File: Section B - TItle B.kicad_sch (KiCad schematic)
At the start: 0 parts

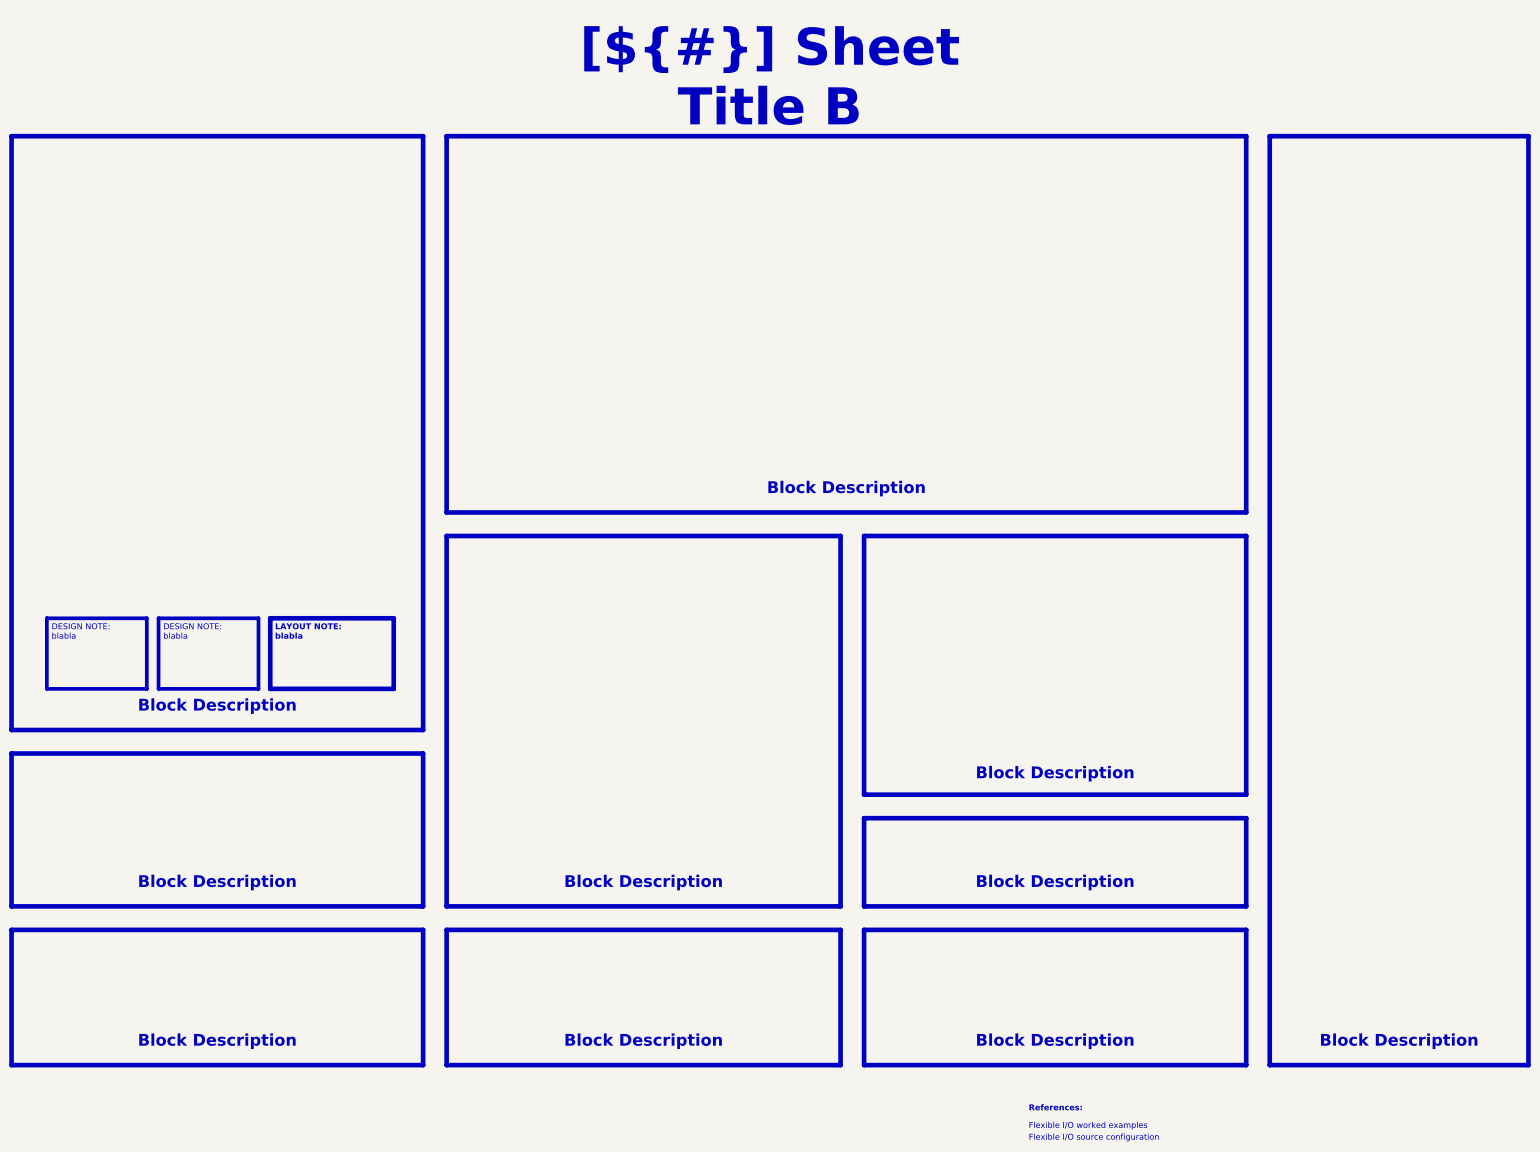
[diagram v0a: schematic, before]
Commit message: Save KiCad 10 design work
Snapshot of the schematic and PCB work done since the initial template
commit: AD7606C-18 ADC, 3x INA241A2 + PBV 1 mOhm shunts, MR60PW phase
connectors, LT8362 boost and LT3045-1 / LTC6655 analog supplies, project
libraries (lib/) and their sym/fp-lib-table.

.gitignore now excludes local history, SpinRender working files, the
stray .step export and Component Search Engine download leftovers.

Co-Authored-By: Claude Opus 5.5 <noreply@anthropic.com>
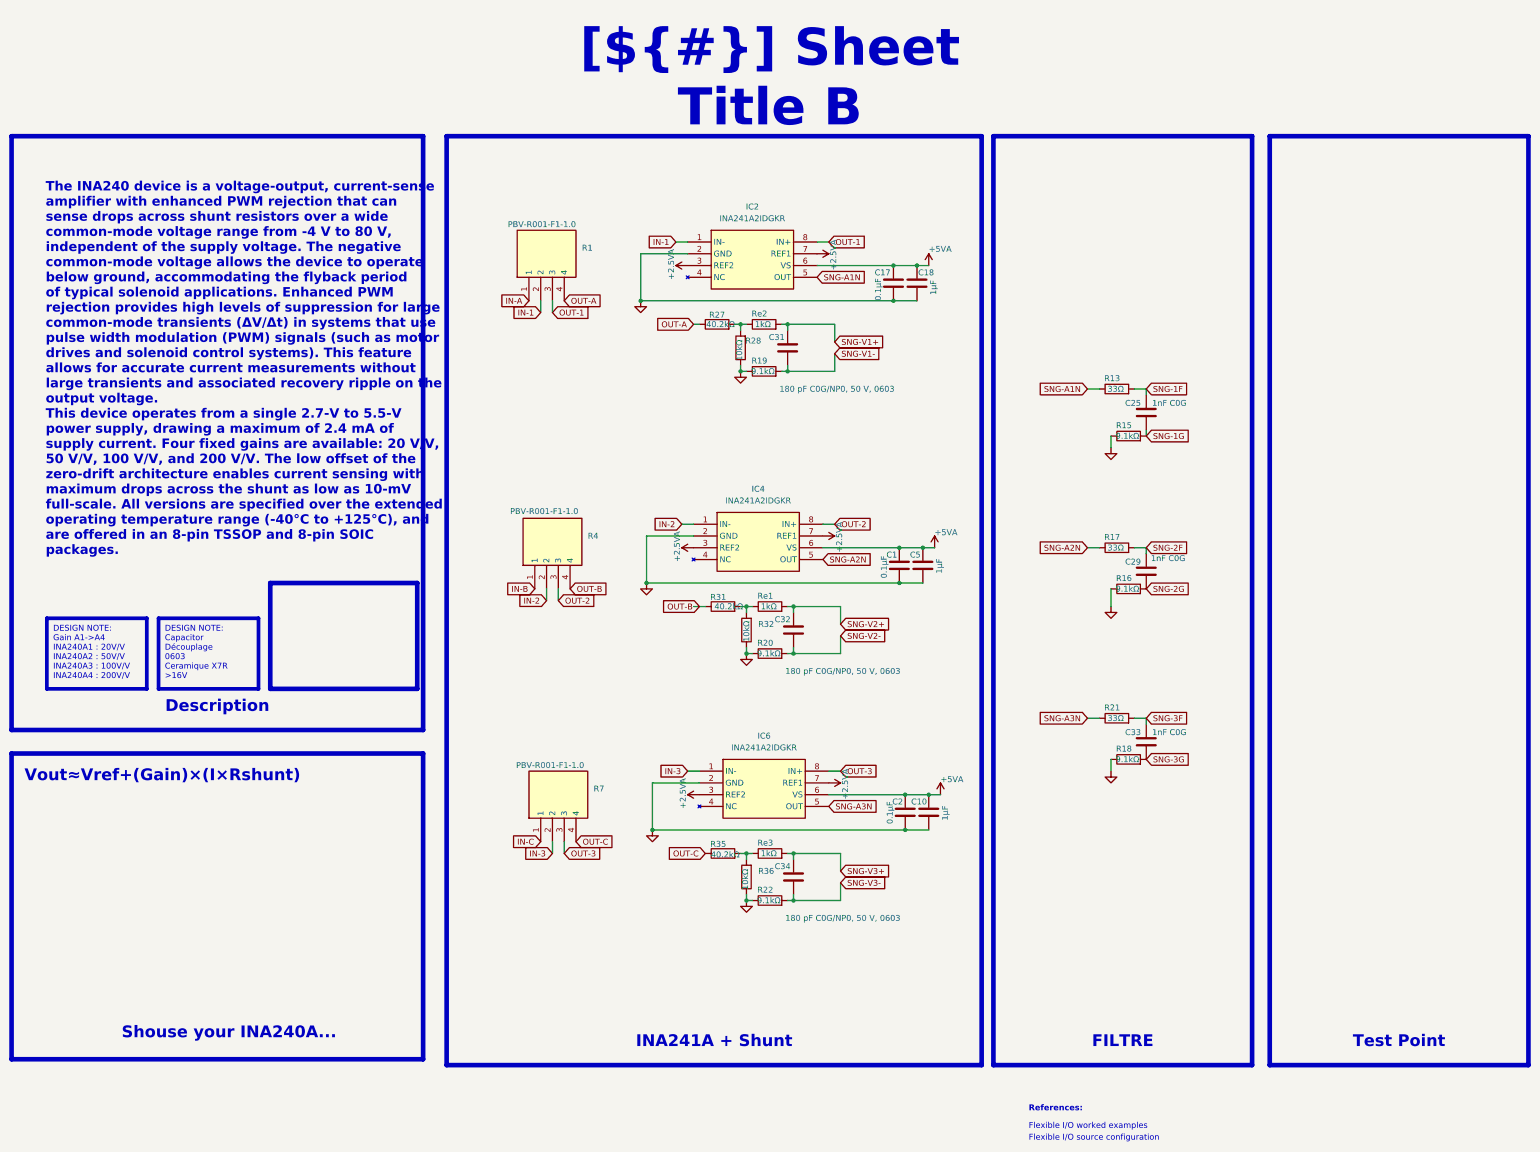
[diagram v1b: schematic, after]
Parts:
- added C1, C17, C2: 0.1µF, Capacitor_SMD:C_0603_1608Metric, symbol Device:C
- added C10, C18, C5: 1µF, Capacitor_SMD:C_0603_1608Metric, symbol Device:C
- added C25, C29, C33: 1nF C0G, Capacitor_SMD:C_0603_1608Metric, symbol Device:C
- added C31, C32, C34: 180 pF C0G/NP0, 50 V, 0603, Capacitor_SMD:C_0603_1608Metric, symbol Device:C
- added IC2, IC4, IC6: INA241A2IDGKR, SOP65P490X110-8N, symbol INA241A2IDGKR:INA241A2IDGKR
- added R1, R4, R7: PBV-R001-F1-1.0, PBVR001F110, symbol PBV-R001-F1-1_0:PBV-R001-F1-1.0
- added R13, R17, R21: 33Ω, Resistor_SMD:R_0603_1608Metric, symbol Device:R
- added R15, R16, R18, R19, R20, R22: 9.1kΩ, Resistor_SMD:R_0603_1608Metric, symbol Device:R
- added R27, R31, R35: 40.2kΩ, Resistor_SMD:R_0805_2012Metric, symbol Device:R
- added R28, R32, R36: 10kΩ, Resistor_SMD:R_0805_2012Metric, symbol Device:R
- added Re1, Re2, Re3: 1kΩ, Resistor_SMD:R_0603_1608Metric, symbol Device:R
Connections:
- new net: R31.2, R32.2, Re1.1
- new net: R27.2, R28.2, Re2.1
- new net: R35.2, R36.2, Re3.1
- new net +2.5VA: IC2.3 (REF2), IC2.7 (REF1), IC4.3 (REF2), IC4.7 (REF1), IC6.3 (REF2), IC6.7 (REF1)
- new net +5VA: C1.1, C10.1, C17.1, C18.1, C2.1, C5.1, IC2.6 (VS), IC4.6 (VS), IC6.6 (VS)
- new net GND: C1.2, C10.2, C17.2, C18.2, C2.2, C5.2, IC2.2 (GND), IC4.2 (GND), IC6.2 (GND), R15.1, R16.1, R18.1, R19.1, R20.1, R22.1, R28.1, R32.1, R36.1
- new net IN-1: IC2.1 (IN-), R1.2
- new net IN-2: IC4.1 (IN-), R4.2
- new net IN-3: IC6.1 (IN-), R7.2
- new net IN-A: R1.1
- new net IN-B: R4.1
- new net IN-C: R7.1
- new net OUT-1: IC2.8 (IN+), R1.3
- new net OUT-2: IC4.8 (IN+), R4.3
- new net OUT-3: IC6.8 (IN+), R7.3
- new net OUT-A: R1.4, R27.1
- new net OUT-B: R31.1, R4.4
- new net OUT-C: R35.1, R7.4
- new net SNG-1F: C25.1, R13.2
- new net SNG-1G: C25.2, R15.2
- new net SNG-2F: C29.1, R17.2
- new net SNG-2G: C29.2, R16.2
- new net SNG-3F: C33.1, R21.2
- new net SNG-3G: C33.2, R18.2
- new net SNG-A1N: IC2.5 (OUT), R13.1
- new net SNG-A2N: IC4.5 (OUT), R17.1
- new net SNG-A3N: IC6.5 (OUT), R21.1
- new net SNG-V1+: C31.1, Re2.2
- new net SNG-V1-: C31.2, R19.2
- new net SNG-V2+: C32.1, Re1.2
- new net SNG-V2-: C32.2, R20.2
- new net SNG-V3+: C34.1, Re3.2
- new net SNG-V3-: C34.2, R22.2
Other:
- note added: "The INA240 device is a voltage-output, current-sense amplifier with enhanced PWM rejection that can sense drops across shunt resistors over a wide common-mode voltage range from -4 V to 80 V, independent of the supply voltage. The negative common-mode voltage allows the device to operate below ground, accommodating the flyback period of typical solenoid applications. Enhanced PWM rejection provid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"
- note added: "Vout≈Vref+(Gain)×(I×Rshunt)"
